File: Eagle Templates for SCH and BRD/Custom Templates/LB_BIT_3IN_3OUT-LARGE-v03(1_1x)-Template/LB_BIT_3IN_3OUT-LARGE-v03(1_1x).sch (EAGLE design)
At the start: 36 parts, among them U1 LV321SOT23-5, U2 LV321SOT23-5, U3 LV321SOT23-5, U4 LV321SOT23-5, U5 LV321SOT23-5, U6 LV321SOT23-5

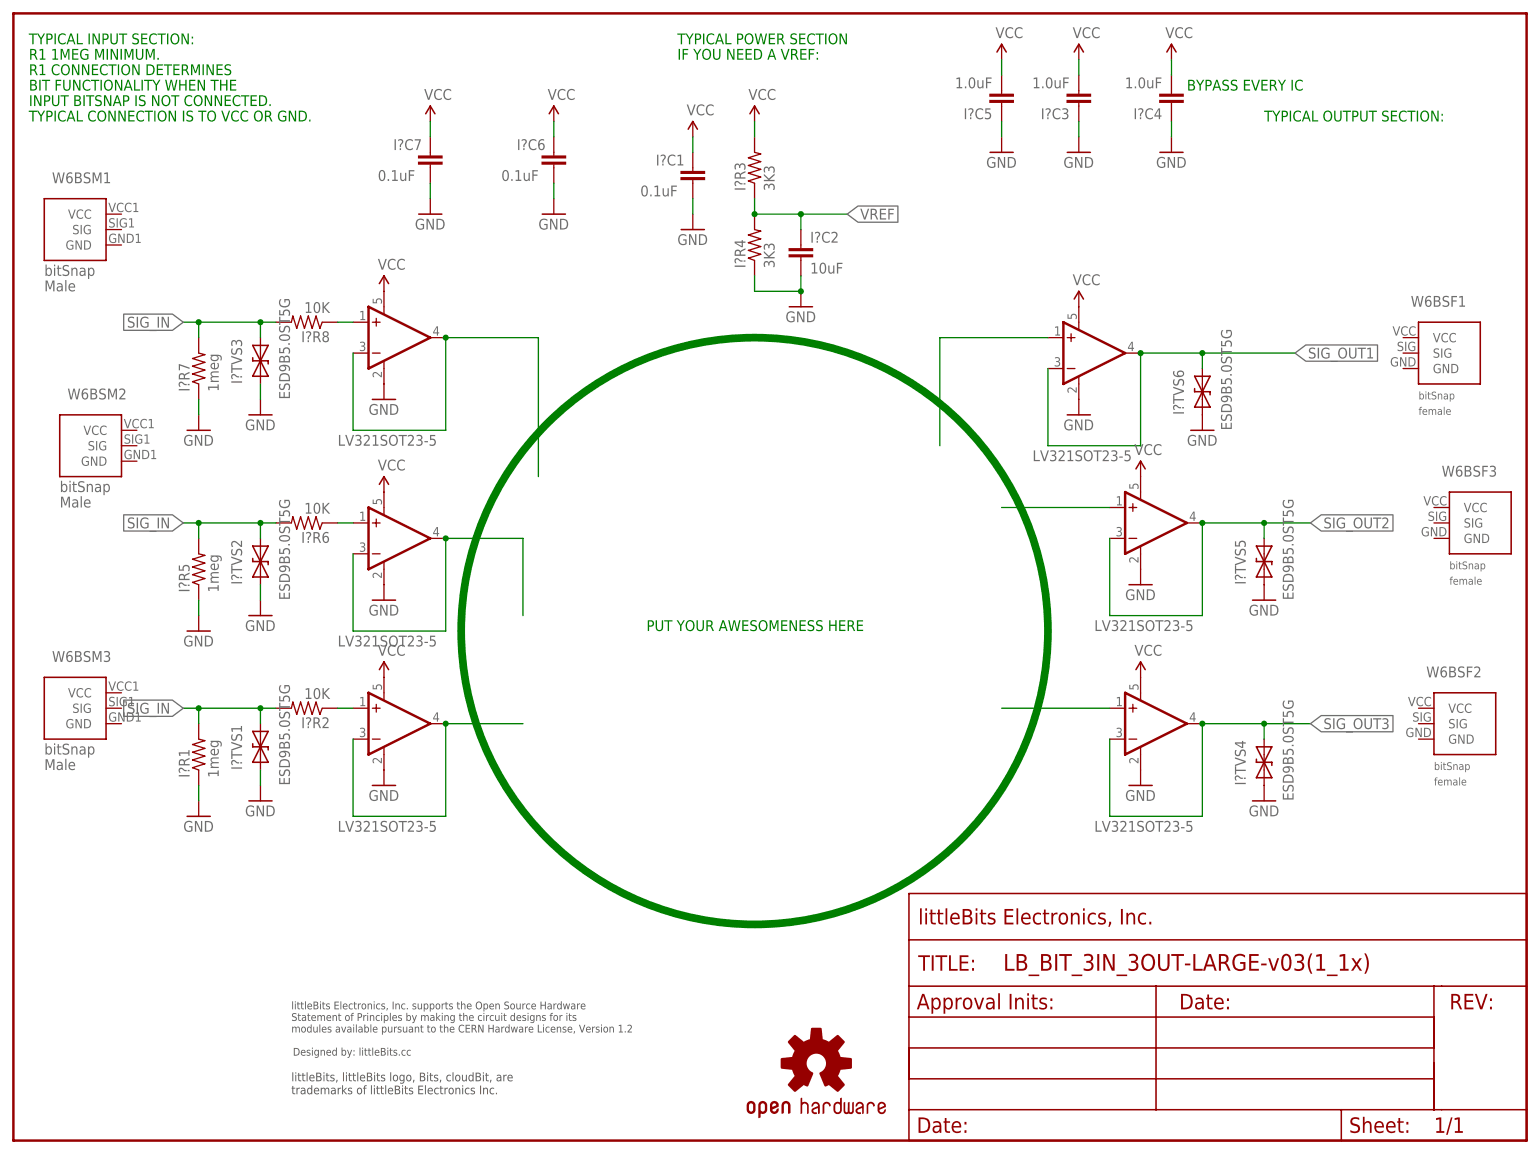
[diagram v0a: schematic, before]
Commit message: Updated templates
- Added ferrite beads
- Moved text and annotations off of Nets layer
- Minor layout changes
- Removed I/O/W prefix from reference designators
- Removed output stage components from output bits
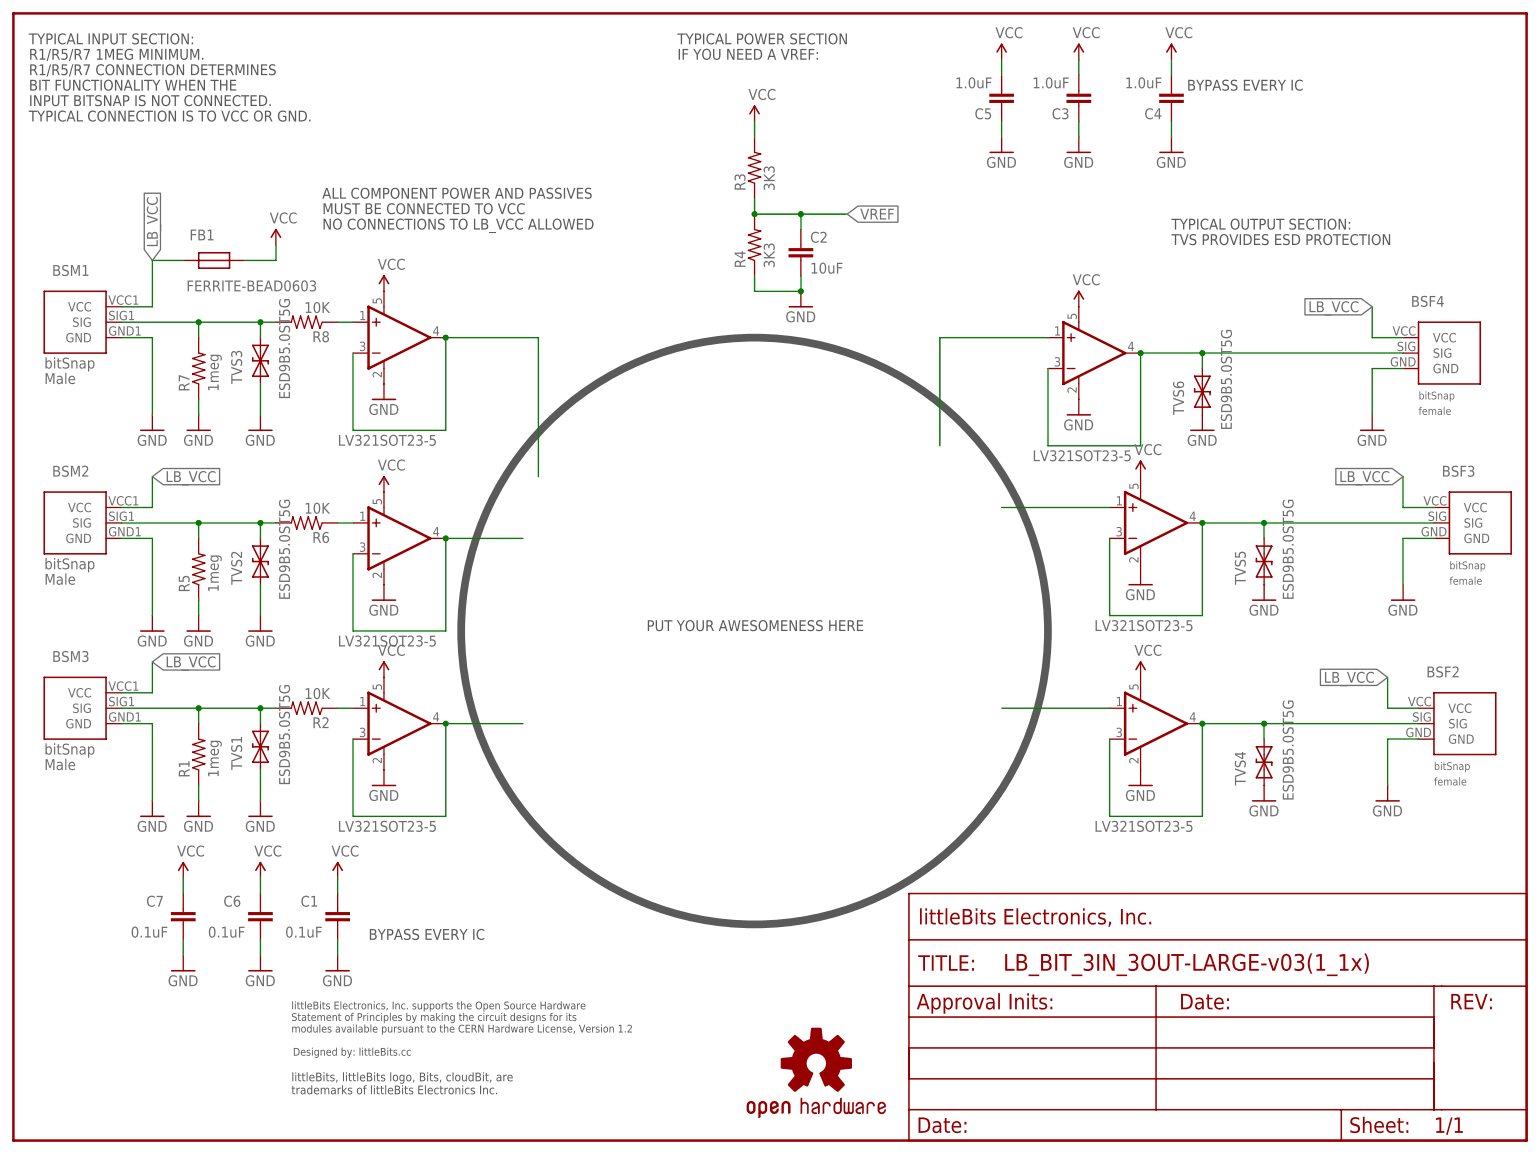
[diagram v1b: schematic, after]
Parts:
- removed I?C1, I?C6, I?C7: 0.1uF, LITTLEBITS:CAPCAP-0603
- removed W6BSM1, W6BSM2: BITSNAP_V03_MALE, bitSnap:BITSNAP_V03_MALE
- added BSM1, BSM2: BITSNAP_V03_MALE, bitSnap:BITSNAP_V03_MALE
- added C1, C6, C7: 0.1uF, LITTLEBITS:CAPCAP-0603
- added FB1: FERRITE-BEAD0603, LITTLEBITS:FERRITE-BEAD0603
- renumbered I?C2 to C2, I?C3 to C3, I?C4 to C4, I?C5 to C5, I?R1 to R1, I?R2 to R2, I?R3 to R3, I?R4 to R4, I?R5 to R5, I?R6 to R6, I?R7 to R7, I?R8 to R8, I?TVS1 to TVS1, I?TVS2 to TVS2, I?TVS3 to TVS3, I?TVS4 to TVS4, I?TVS5 to TVS5, I?TVS6 to TVS6, W6BSF1 to BSF4, W6BSF2 to BSF2, W6BSF3 to BSF3, W6BSM3 to BSM3
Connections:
- removed net SIG_IN: R1.2, R2.2, R5.2, R6.2, R7.2, R8.2, TVS1.C, TVS2.C, TVS3.C
- new net LB_VCC: BSF2.VCC, BSF3.VCC, BSF4.VCC, BSM1.VCC, BSM2.VCC, BSM3.VCC, FB1.P$2
- new net N$3: BSM1.SIG, R7.2, R8.2, TVS3.C
- new net N$4: BSM2.SIG, R5.2, R6.2, TVS2.C
- new net N$5: BSM3.SIG, R1.2, R2.2, TVS1.C
- net GND: now also BSF2.GND, BSF3.GND, BSF4.GND, BSM1.GND, BSM2.GND, BSM3.GND, C1.2, C6.2, C7.2; no longer I?C1.2, I?C6.2, I?C7.2
- net SIG_OUT1: now also BSF4.SIG
- net SIG_OUT2: now also BSF3.SIG
- net SIG_OUT3: now also BSF2.SIG
- net VCC: now also C1.1, C6.1, C7.1, FB1.P$1; no longer I?C1.1, I?C6.1, I?C7.1
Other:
- note added: "ALL COMPONENT POWER AND PASSIVES"
- note added: "MUST BE CONNECTED TO VCC"
- note added: "NO CONNECTIONS TO LB_VCC ALLOWED"
- note added: "R1/R5/R7 1MEG MINIMUM."
- note added: "R1/R5/R7 CONNECTION DETERMINES"
- note added: "TVS PROVIDES ESD PROTECTION"
- note removed: "R1 1MEG MINIMUM."
- note removed: "R1 CONNECTION DETERMINES"
